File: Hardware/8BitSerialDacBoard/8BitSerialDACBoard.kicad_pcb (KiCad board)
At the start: 4 copper layers, 27 x 16 mm, 29 parts, among them J1 Conn_01x08, U1 SN74LV595APWRG4

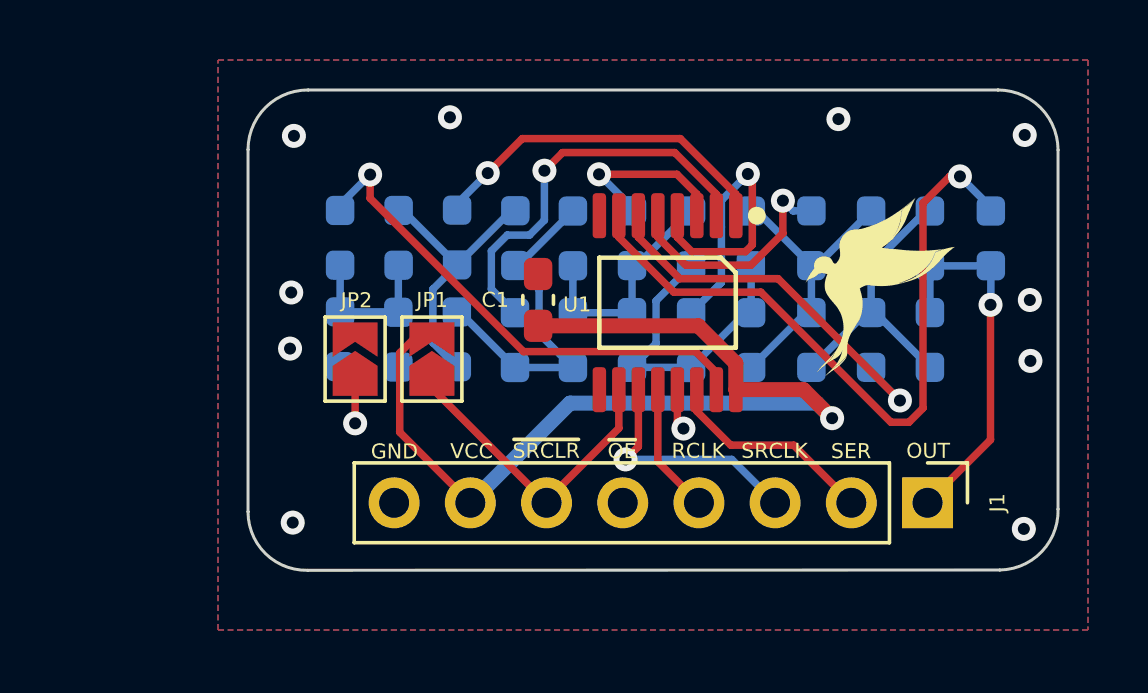
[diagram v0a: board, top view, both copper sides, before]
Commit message: Adding chainablity to DACs, need to flip bit direction
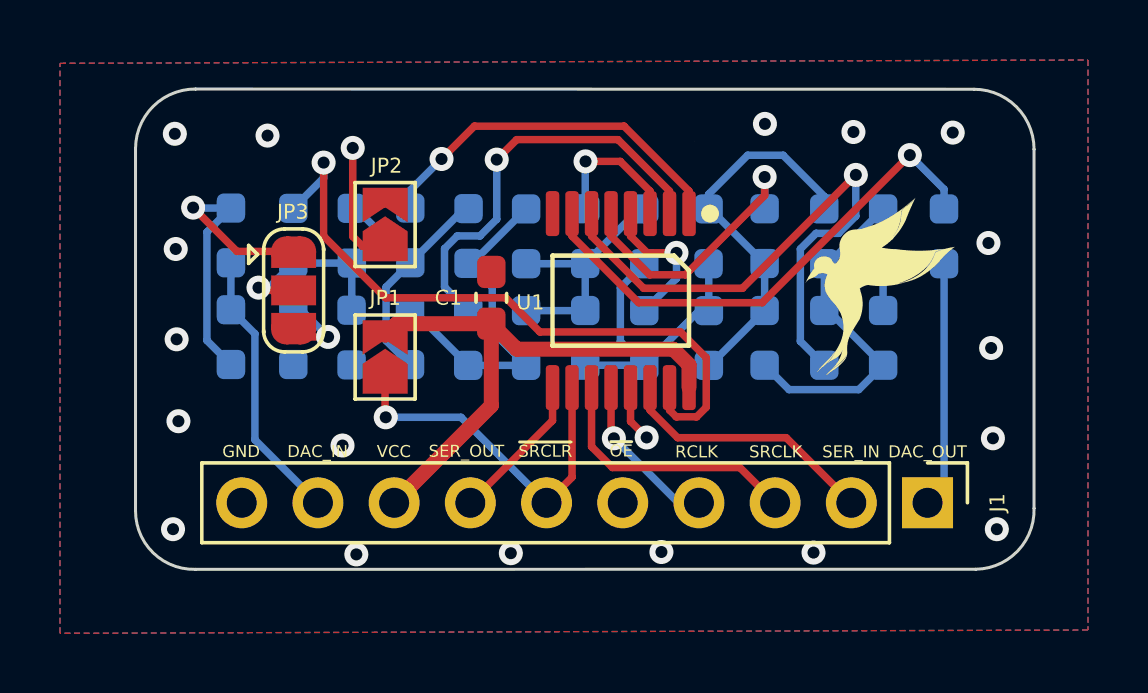
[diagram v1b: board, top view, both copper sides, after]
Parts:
- added JP3: SolderJumper_3_Open, Jumper:SolderJumper-3_P1.3mm_Open_RoundedPad1.0x1.5mm, F.Cu at (128.2, 94.2)
- added R24: R_Small_US, Resistor_SMD:R_0603_1608Metric_Pad0.98x0.95mm_HandSolder, B.Cu at (126.2, 92.4)
- added R25: R_Small_US, Resistor_SMD:R_0603_1608Metric_Pad0.98x0.95mm_HandSolder, B.Cu at (126.2, 95.8)
- J1: value Conn_01x08 -> Conn_01x10; footprint Connector_PinHeader_2.54mm:PinHeader_1x08_P2.54mm_Vertical -> Connector_PinHeader_2.54mm:PinHeader_1x10_P2.54mm_Vertical
- moved JP2 4.60 mm to (131.3, 92.0)
- moved JP1 1.56 mm to (131.3, 96.4)
- moved R1 1.56 mm to (128.2, 92.4)
- moved R11 1.56 mm to (138.0, 92.4)
- moved R12 1.56 mm to (138.0, 95.8)
- moved R17 1.56 mm to (143.9, 92.4)
- moved R18 1.56 mm to (143.9, 95.8)
- moved R20 1.56 mm to (145.9, 95.8)
- moved R22 1.56 mm to (147.9, 95.8)
- moved R3 1.56 mm to (130.2, 92.4)
- moved R6 1.56 mm to (132.1, 95.8)
- moved R7 1.56 mm to (134.1, 92.4)
- moved R10 1.56 mm to (136.0, 95.8)
- moved R13 1.56 mm to (139.9, 92.4)
- moved R14 1.56 mm to (139.9, 95.8)
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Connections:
- J1 pad 7: VCC -> SER_OUT
- J1 pad 8: GND -> VCC
- R1 pad 2: Net-(R1-Pad2) -> Net-(JP3-C)
- R2 pad 1: Net-(R1-Pad2) -> Net-(JP3-B)
- R3 pad 1: Net-(R1-Pad2) -> Net-(JP3-C)
- R4 pad 1: Net-(R1-Pad2) -> Net-(JP3-C)
- U1 pad 9: unconnected-(U1-Pad9) -> SER_OUT
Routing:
- net VCC: track 32.5 -> 18.9 mm, vias 1 -> 0
- net Net-(JP3-A): track 0.00 -> 11.1 mm, vias 0 -> 1
- net DAC_IN: track 0.00 -> 9.20 mm
- net Net-(U1-QG): track 13.2 -> 19.7 mm
- net Net-(U1-QE): track 11.3 -> 4.88 mm
- net Net-(U1-QH): track 23.6 -> 17.2 mm
- net Net-(JP3-C): track 0.00 -> 6.23 mm, vias 0 -> 1
- net Net-(J1-Pin_5): track 16.1 -> 22.4 mm
- net Net-(U1-QA): track 16.9 -> 22.7 mm
- net Net-(R1-Pad2): track 5.08 -> 0.00 mm
- net SER_OUT: track 0.00 -> 4.97 mm
- net Net-(R15-Pad2): track 9.85 -> 12.7 mm
- net Net-(JP3-B): track 0.00 -> 2.79 mm, vias 0 -> 1
- net Net-(R18-Pad2): track 9.74 -> 11.9 mm
- net Net-(J1-Pin_6): track 10.4 -> 12.0 mm, vias 0 -> 1
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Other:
- board size 27 x 16 mm -> 29.9 x 16 mm
- board text added: "DAC_IN"
- board text added: "DAC_OUT"
- board text added: "SER_IN"
- board text added: "SER_OUT"
- board text removed: "OUT"
- board text removed: "SER"
